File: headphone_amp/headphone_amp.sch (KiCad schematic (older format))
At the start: 40 parts, among them J1 Molex_SL_01x02_Male, J2 Molex_SL_01x02_Male, J3 Molex_SL_01x03_Male, J4 Molex_SL_01x03_Male, Q1 PZTA42, Q2 PZTA92, Q3 PZTA42, Q4 PZTA92, U1 NE5532

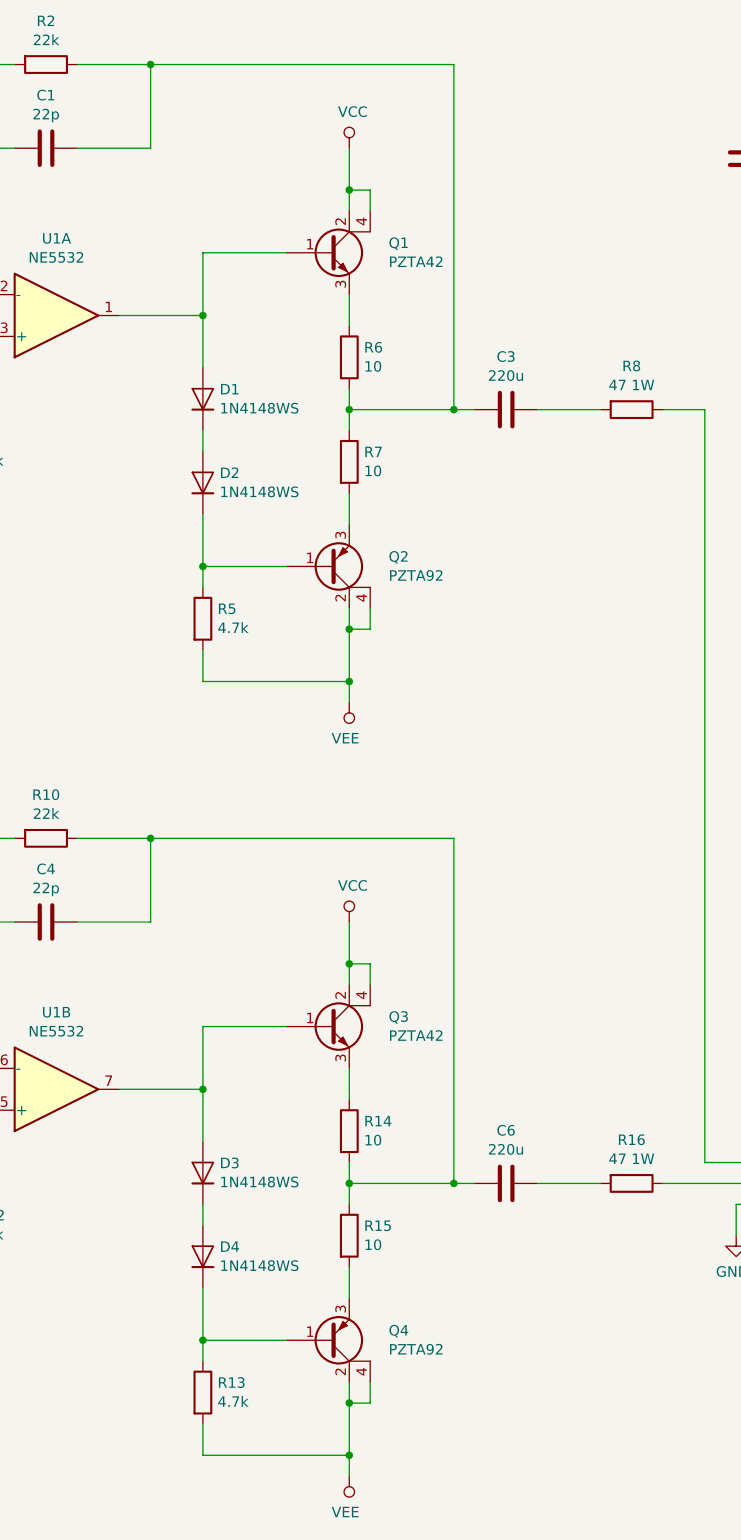
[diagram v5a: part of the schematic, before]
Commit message: update output transistor symbols/footprints
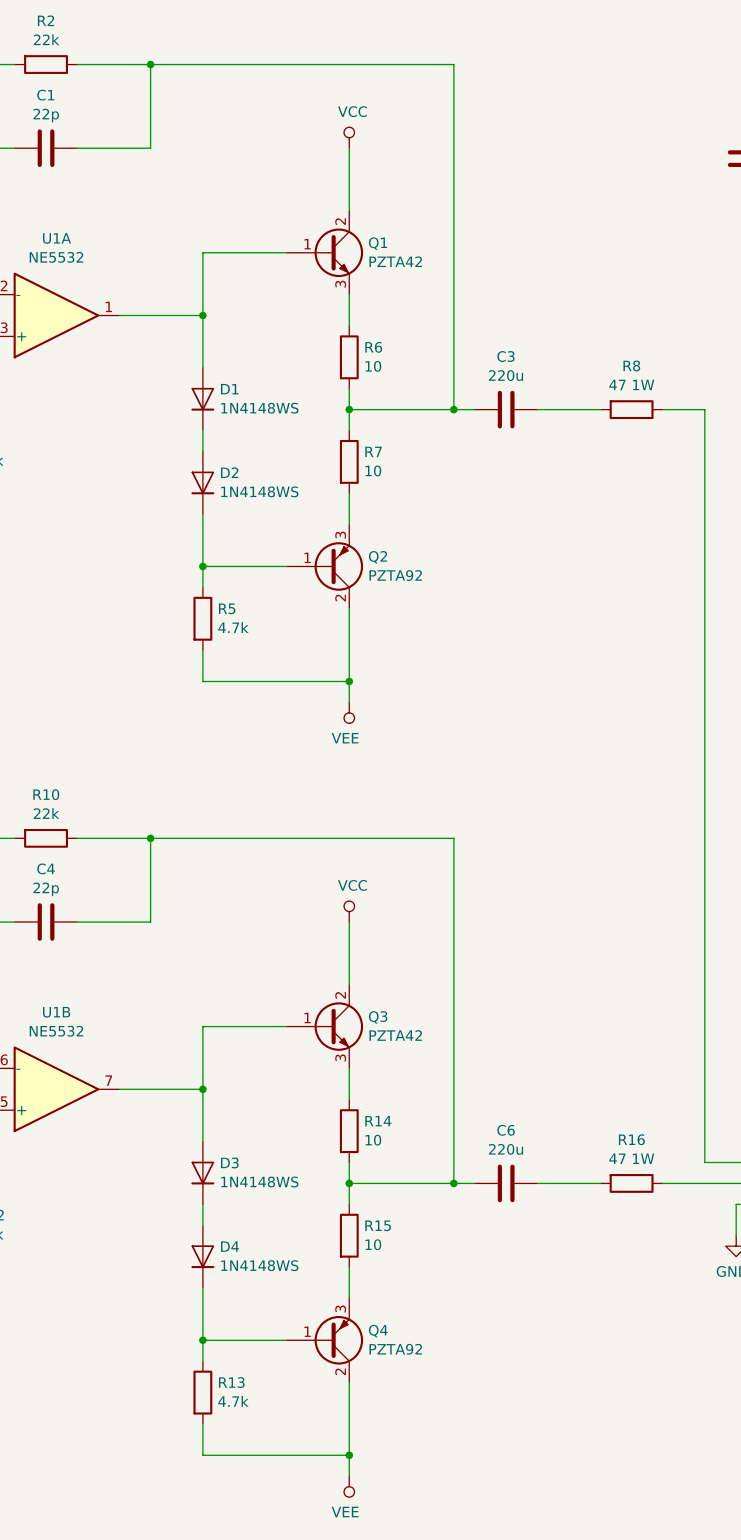
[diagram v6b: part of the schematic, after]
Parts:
- removed Q1, Q3: PZTA42, Package_TO_SOT_SMD:SOT-223, symbol Device:Q_NPN_BCEC
- removed Q2, Q4: PZTA92, Package_TO_SOT_SMD:SOT-223, symbol Device:Q_PNP_BCEC
- added Q1, Q3: PZTA42, Package_TO_SOT_SMD:SOT-223-3_TabPin2, symbol Transistor_BJT_gkeeth:PZTA42
- added Q2, Q4: PZTA92, Package_TO_SOT_SMD:SOT-223-3_TabPin2, symbol Transistor_BJT:PZTA92
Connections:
- net VCC: now also Q1.2 (C), Q3.2 (C)
- net VEE: now also Q2.2 (C), Q4.2 (C)
- net at R6.1: now also Q1.3 (E)
- net at R7.2: now also Q2.3 (E)
- net at D1.2 (A), U1.1: now also Q1.1 (B)
- net at D2.1 (K), R5.1: now also Q2.1 (B)
- net at R14.1: now also Q3.3 (E)
- net at R15.2: now also Q4.3 (E)
- net at D3.2 (A), U1.7: now also Q3.1 (B)
- net at D4.1 (K), R13.1: now also Q4.1 (B)
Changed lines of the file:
@@
 	4600 2650 4600 2750
-Wire Wire Line
-	4600 3050 4600 3300
-Wire Wire Line
-	5000 3300 4600 3300
-Connection ~ 4600 3300
-Wire Wire Line
-	4600 3300 4600 3400
-Wire Wire Line
-	5300 3100 5300 2950
 Wire Wire Line
 	5300 2650 5300 2550
@@
 Wire Wire Line
 	4600 3850 5300 3850
-Connection ~ 5300 3850
-Wire Wire Line
-	5300 3850 5300 3600
-Wire Wire Line
-	5300 1600 5300 1500
 $Comp
 L Device:R R2
@@
 	4600 7550 5300 7550
 Connection ~ 5300 7550
-Wire Wire Line
-	5300 7550 5300 7300
-Wire Wire Line
-	5300 5300 5300 5200
 $Comp
 L Device:R R12
@@
 $EndComp
 $Comp
-L Device:Q_PNP_BCEC Q2
-U 1 1 5D96CA9F
-P 5200 3300
-F 0 "Q2" H 5488 3254 50  0000 L CNN
-F 1 "PZTA92" H 5488 3345 50  0000 L CNN
-F 2 "Package_TO_SOT_SMD:SOT-223" H 5400 3400 50  0001 C CNN
-F 3 "https://www.onsemi.com/pub/Collateral/PZTA92T1-D.PDF" H 5200 3300 50  0001 C CNN
-F 4 "ON Semiconductor" H 5200 3300 50  0001 C CNN "Manufacturer"
-F 5 "PZTA92T1G" H 5200 3300 50  0001 C CNN "Manufacturer PN"
-F 6 "Digikey" H 5200 3300 50  0001 C CNN "Distributor"
-F 7 "PZTA92T1GOSCT-ND" H 5200 3300 50  0001 C CNN "Distributor PN"
-F 8 "https://www.digikey.com/product-detail/en/on-semiconductor/PZTA92T1G/PZTA92T1GOSCT-ND/920290" H 5200 3300 50  0001 C CNN "URL"
-F 9 "0.44" H 5200 3300 50  0001 C CNN "Unit Price"
-	1    5200 3300
-	1    0    0    1
-$EndComp
-$Comp
-L Device:Q_NPN_BCEC Q3
-U 1 1 5D973B3C
-P 5200 5500
-F 0 "Q3" H 5488 5546 50  0000 L CNN
-F 1 "PZTA42" H 5488 5455 50  0000 L CNN
-F 2 "Package_TO_SOT_SMD:SOT-223" H 5400 5600 50  0001 C CNN
-F 3 "https://www.onsemi.com/pub/Collateral/PZTA42T1-D.PDF" H 5200 5500 50  0001 C CNN
-F 4 "ON Semiconductor" H 5200 5500 50  0001 C CNN "Manufacturer"
-F 5 "Digikey" H 5200 5500 50  0001 C CNN "Distributor"
-F 6 "PZTA42T1GOSCT-ND" H 5200 5500 50  0001 C CNN "Distributor PN"
-F 7 "PZTA42T1G" H 5200 5500 50  0001 C CNN "Manufacturer PN"
-F 8 "https://www.digikey.com/product-detail/en/on-semiconductor/PZTA42T1G/PZTA42T1GOSCT-ND/1139989" H 5200 5500 50  0001 C CNN "URL"
-F 9 "0.43" H 5200 5500 50  0001 C CNN "Unit Price"
-	1    5200 5500
-	1    0    0    -1
-$EndComp
-Wire Wire Line
-	5300 5200 5400 5200
-Wire Wire Line
-	5400 5200 5400 5300
-Connection ~ 5300 5200
-Wire Wire Line
-	5300 5200 5300 5000
-$Comp
-L Device:Q_NPN_BCEC Q1
-U 1 1 5D97BBB9
-P 5200 1800
-F 0 "Q1" H 5488 1846 50  0000 L CNN
-F 1 "PZTA42" H 5488 1755 50  0000 L CNN
-F 2 "Package_TO_SOT_SMD:SOT-223" H 5400 1900 50  0001 C CNN
-F 3 "https://www.onsemi.com/pub/Collateral/PZTA42T1-D.PDF" H 5200 1800 50  0001 C CNN
-F 4 "ON Semiconductor" H 5200 1800 50  0001 C CNN "Manufacturer"
-F 5 "Digikey" H 5200 1800 50  0001 C CNN "Distributor"
-F 6 "PZTA42T1GOSCT-ND" H 5200 1800 50  0001 C CNN "Distributor PN"
-F 7 "PZTA42T1G" H 5200 1800 50  0001 C CNN "Manufacturer PN"
-F 8 "https://www.digikey.com/product-detail/en/on-semiconductor/PZTA42T1G/PZTA42T1GOSCT-ND/1139989" H 5200 1800 50  0001 C CNN "URL"
-F 9 "0.43" H 5200 1800 50  0001 C CNN "Unit Price"
-	1    5200 1800
-	1    0    0    -1
-$EndComp
-Wire Wire Line
-	5400 1600 5400 1500
-Wire Wire Line
-	5400 1500 5300 1500
-Connection ~ 5300 1500
-Wire Wire Line
-	5300 1500 5300 1300
-$Comp
-L Device:Q_PNP_BCEC Q4
-U 1 1 5D98233C
-P 5200 7000
-F 0 "Q4" H 5488 6954 50  0000 L CNN
-F 1 "PZTA92" H 5488 7045 50  0000 L CNN
-F 2 "Package_TO_SOT_SMD:SOT-223" H 5400 7100 50  0001 C CNN
-F 3 "https://www.onsemi.com/pub/Collateral/PZTA92T1-D.PDF" H 5200 7000 50  0001 C CNN
-F 4 "ON Semiconductor" H 5200 7000 50  0001 C CNN "Manufacturer"
-F 5 "PZTA92T1G" H 5200 7000 50  0001 C CNN "Manufacturer PN"
-F 6 "Digikey" H 5200 7000 50  0001 C CNN "Distributor"
-F 7 "PZTA92T1GOSCT-ND" H 5200 7000 50  0001 C CNN "Distributor PN"
-F 8 "https://www.digikey.com/product-detail/en/on-semiconductor/PZTA92T1G/PZTA92T1GOSCT-ND/920290" H 5200 7000 50  0001 C CNN "URL"
-F 9 "0.44" H 5200 7000 50  0001 C CNN "Unit Price"
-	1    5200 7000
-	1    0    0    1
-$EndComp
-Wire Wire Line
-	5400 3500 5400 3600
-Wire Wire Line
-	5400 3600 5300 3600
-Connection ~ 5300 3600
-Wire Wire Line
-	5300 3600 5300 3500
-Wire Wire Line
-	5400 7200 5400 7300
-Wire Wire Line
-	5400 7300 5300 7300
-Connection ~ 5300 7300
-Wire Wire Line
-	5300 7300 5300 7200
-$Comp
 L Device:R R16
 U 1 1 5D99AC16
@@
 	0    1    1    0
 $EndComp
+Wire Wire Line
+	5300 1300 5300 1600
+$Comp
+L Transistor_BJT_gkeeth:PZTA42 Q1
+U 1 1 5D835D77
+P 5200 1800
+F 0 "Q1" H 5390 1846 50  0000 L CNN
+F 1 "PZTA42" H 5390 1755 50  0000 L CNN
+F 2 "Package_TO_SOT_SMD:SOT-223-3_TabPin2" H 5400 1725 50  0001 L CIN
+F 3 "https://www.onsemi.com/pub/Collateral/PZTA42T1-D.PDF" H 5200 1800 50  0001 L CNN
+F 4 "Digikey" H 5200 1800 50  0001 C CNN "Distributor"
+F 5 "PZTA42T1GOSCT-ND" H 5200 1800 50  0001 C CNN "Distributor PN"
+F 6 "ON Semiconductor" H 5200 1800 50  0001 C CNN "Manufacturer"
+F 7 "PZTA42T1G" H 5200 1800 50  0001 C CNN "Manufacturer PN"
+F 8 "https://www.digikey.com/product-detail/en/on-semiconductor/PZTA42T1G/PZTA42T1GOSCT-ND/1139989" H 5200 1800 50  0001 C CNN "URL"
+F 9 "0.43" H 5200 1800 50  0001 C CNN "Unit Price"
+	1    5200 1800
+	1    0    0    -1
+$EndComp
+Connection ~ 5300 3850
+Wire Wire Line
+	5300 3100 5300 2950
+Wire Wire Line
+	4600 3300 4600 3400
+Wire Wire Line
+	4600 3050 4600 3300
+Connection ~ 4600 3300
+Wire Wire Line
+	5000 3300 4600 3300
+$Comp
+L Transistor_BJT:PZTA92 Q2
+U 1 1 5D83FFA6
+P 5200 3300
+F 0 "Q2" H 5390 3254 50  0000 L CNN
+F 1 "PZTA92" H 5390 3345 50  0000 L CNN
+F 2 "Package_TO_SOT_SMD:SOT-223-3_TabPin2" H 5400 3225 50  0001 L CIN
+F 3 "https://www.onsemi.com/pub/Collateral/PZTA92T1-D.PDF" H 5200 3300 50  0001 L CNN
+F 4 "Digikey" H 5200 3300 50  0001 C CNN "Distributor"
+F 5 "PZTA92T1GOSCT-ND" H 5200 3300 50  0001 C CNN "Distributor PN"
+F 6 "ON Semiconductor" H 5200 3300 50  0001 C CNN "Manufacturer"
+F 7 "PZTA92T1G" H 5200 3300 50  0001 C CNN "Manufacturer PN"
+F 8 "https://www.digikey.com/product-detail/en/on-semiconductor/PZTA92T1G/PZTA92T1GOSCT-ND/920290" H 5200 3300 50  0001 C CNN "URL"
+F 9 "0.44" H 5200 3300 50  0001 C CNN "Unit Price"
+	1    5200 3300
+	1    0    0    1
+$EndComp
+Wire Wire Line
+	5300 3500 5300 3850
+Wire Wire Line
+	5300 7200 5300 7550
+Wire Wire Line
+	5300 5000 5300 5300
+$Comp
+L Transistor_BJT:PZTA92 Q4
+U 1 1 5D846814
+P 5200 7000
+F 0 "Q4" H 5390 6954 50  0000 L CNN
+F 1 "PZTA92" H 5390 7045 50  0000 L CNN
+F 2 "Package_TO_SOT_SMD:SOT-223-3_TabPin2" H 5400 6925 50  0001 L CIN
+F 3 "https://www.onsemi.com/pub/Collateral/PZTA92T1-D.PDF" H 5200 7000 50  0001 L CNN
+F 4 "Digikey" H 5200 7000 50  0001 C CNN "Distributor"
+F 5 "PZTA92T1GOSCT-ND" H 5200 7000 50  0001 C CNN "Distributor PN"
+F 6 "ON Semiconductor" H 5200 7000 50  0001 C CNN "Manufacturer"
+F 7 "PZTA92T1G" H 5200 7000 50  0001 C CNN "Manufacturer PN"
+F 8 "https://www.digikey.com/product-detail/en/on-semiconductor/PZTA92T1G/PZTA92T1GOSCT-ND/920290" H 5200 7000 50  0001 C CNN "URL"
+F 9 "0.44" H 5200 7000 50  0001 C CNN "Unit Price"
+	1    5200 7000
+	1    0    0    1
+$EndComp
+$Comp
+L Transistor_BJT_gkeeth:PZTA42 Q3
+U 1 1 5D8472CD
+P 5200 5500
+F 0 "Q3" H 5390 5546 50  0000 L CNN
+F 1 "PZTA42" H 5390 5455 50  0000 L CNN
+F 2 "Package_TO_SOT_SMD:SOT-223-3_TabPin2" H 5400 5425 50  0001 L CIN
+F 3 "https://www.onsemi.com/pub/Collateral/PZTA42T1-D.PDF" H 5200 5500 50  0001 L CNN
+F 4 "Digikey" H 5200 5500 50  0001 C CNN "Distributor"
+F 5 "PZTA42T1GOSCT-ND" H 5200 5500 50  0001 C CNN "Distributor PN"
+F 6 "ON Semiconductor" H 5200 5500 50  0001 C CNN "Manufacturer"
+F 7 "PZTA42T1G" H 5200 5500 50  0001 C CNN "Manufacturer PN"
+F 8 "https://www.digikey.com/product-detail/en/on-semiconductor/PZTA42T1G/PZTA42T1GOSCT-ND/1139989" H 5200 5500 50  0001 C CNN "URL"
+F 9 "0.43" H 5200 5500 50  0001 C CNN "Unit Price"
+	1    5200 5500
+	1    0    0    -1
+$EndComp
 $EndSCHEMATC

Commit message: change output transistors to std lib versions (now in upstream)
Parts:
- removed Q1, Q3: PZTA42, Package_TO_SOT_SMD:SOT-223-3_TabPin2, symbol Transistor_BJT_gkeeth:PZTA42
- added Q1, Q3: PZTA42, Package_TO_SOT_SMD:SOT-223-3_TabPin2, symbol Transistor_BJT:PZTA42
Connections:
- net VCC: now also Q1.2 (C), Q3.2 (C)
- net at R6.1: now also Q1.3 (E)
- net at D1.2 (A), U1.1: now also Q1.1 (B)
- net at R14.1: now also Q3.3 (E)
- net at D3.2 (A), U1.7: now also Q3.1 (B)
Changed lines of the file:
@@
 Wire Wire Line
 	5300 1300 5300 1600
+Connection ~ 5300 3850
+Wire Wire Line
+	5300 3100 5300 2950
+Wire Wire Line
+	4600 3300 4600 3400
+Wire Wire Line
+	4600 3050 4600 3300
+Connection ~ 4600 3300
+Wire Wire Line
+	5000 3300 4600 3300
+Wire Wire Line
+	5300 3500 5300 3850
+Wire Wire Line
+	5300 7200 5300 7550
+Wire Wire Line
+	5300 5000 5300 5300
 $Comp
-L Transistor_BJT_gkeeth:PZTA42 Q1
-U 1 1 5D835D77
+L Transistor_BJT:PZTA42 Q1
+U 1 1 5D86B1D4
 P 5200 1800
 F 0 "Q1" H 5390 1846 50  0000 L CNN
@@
 	1    0    0    -1
 $EndComp
-Connection ~ 5300 3850
-Wire Wire Line
-	5300 3100 5300 2950
-Wire Wire Line
-	4600 3300 4600 3400
-Wire Wire Line
-	4600 3050 4600 3300
-Connection ~ 4600 3300
-Wire Wire Line
-	5000 3300 4600 3300
 $Comp
 L Transistor_BJT:PZTA92 Q2
-U 1 1 5D83FFA6
+U 1 1 5D86C06E
 P 5200 3300
 F 0 "Q2" H 5390 3254 50  0000 L CNN
@@
 	1    0    0    1
 $EndComp
-Wire Wire Line
-	5300 3500 5300 3850
-Wire Wire Line
-	5300 7200 5300 7550
-Wire Wire Line
-	5300 5000 5300 5300
+$Comp
+L Transistor_BJT:PZTA42 Q3
+U 1 1 5D86E452
+P 5200 5500
+F 0 "Q3" H 5390 5546 50  0000 L CNN
+F 1 "PZTA42" H 5390 5455 50  0000 L CNN
+F 2 "Package_TO_SOT_SMD:SOT-223-3_TabPin2" H 5400 5425 50  0001 L CIN
+F 3 "https://www.onsemi.com/pub/Collateral/PZTA42T1-D.PDF" H 5200 5500 50  0001 L CNN
+F 4 "Digikey" H 5200 5500 50  0001 C CNN "Distributor"
+F 5 "PZTA42T1GOSCT-ND" H 5200 5500 50  0001 C CNN "Distributor PN"
+F 6 "ON Semiconductor" H 5200 5500 50  0001 C CNN "Manufacturer"
+F 7 "PZTA42T1G" H 5200 5500 50  0001 C CNN "Manufacturer PN"
+F 8 "https://www.digikey.com/product-detail/en/on-semiconductor/PZTA42T1G/PZTA42T1GOSCT-ND/1139989" H 5200 5500 50  0001 C CNN "URL"
+F 9 "0.43" H 5200 5500 50  0001 C CNN "Unit Price"
+	1    5200 5500
+	1    0    0    -1
+$EndComp
 $Comp
 L Transistor_BJT:PZTA92 Q4
-U 1 1 5D846814
+U 1 1 5D86F45B
 P 5200 7000
 F 0 "Q4" H 5390 6954 50  0000 L CNN
@@
 	1    0    0    1
 $EndComp
-$Comp
-L Transistor_BJT_gkeeth:PZTA42 Q3
-U 1 1 5D8472CD
-P 5200 5500
-F 0 "Q3" H 5390 5546 50  0000 L CNN
-F 1 "PZTA42" H 5390 5455 50  0000 L CNN
-F 2 "Package_TO_SOT_SMD:SOT-223-3_TabPin2" H 5400 5425 50  0001 L CIN
-F 3 "https://www.onsemi.com/pub/Collateral/PZTA42T1-D.PDF" H 5200 5500 50  0001 L CNN
-F 4 "Digikey" H 5200 5500 50  0001 C CNN "Distributor"
-F 5 "PZTA42T1GOSCT-ND" H 5200 5500 50  0001 C CNN "Distributor PN"
-F 6 "ON Semiconductor" H 5200 5500 50  0001 C CNN "Manufacturer"
-F 7 "PZTA42T1G" H 5200 5500 50  0001 C CNN "Manufacturer PN"
-F 8 "https://www.digikey.com/product-detail/en/on-semiconductor/PZTA42T1G/PZTA42T1GOSCT-ND/1139989" H 5200 5500 50  0001 C CNN "URL"
-F 9 "0.43" H 5200 5500 50  0001 C CNN "Unit Price"
-	1    5200 5500
-	1    0    0    -1
-$EndComp
 $EndSCHEMATC

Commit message: Remove output resistors
- remove output resistors for zero ohm output impedance
- add 10k pulldown/bleeder resistors on output to prevent output cap
charging with no load
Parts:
- R16, R8: value 47 1W -> 10k; footprint Resistor_THT:R_Axial_DIN0414_L11.9mm_D4.5mm_P15.24mm_Horizontal -> Resistor_SMD:R_0603_1608Metric_Pad1.05x0.95mm_HandSolder; Distributor Digikey -> (none); Distributor PN BC4537CT-ND -> (none); Manufacturer Vishay BC -> (none); Manufacturer PN MBE04140C4709FC100 -> (none); URL https://www.digikey.com/product-detail/en/vishay-bc-compone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 -> (none); Unit Price 0.69 -> (none)
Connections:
- net GNDA: now also R16.2, R8.2
- net left_out: now also C3.1
- net right_out: now also C6.1
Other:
- note added: "TODO\nconsider other opamps, especially lm4562 and TL072\nheadphone jack ground to chassis...?\nadjust system gain to match headphone volume to speaker volume"
- note added: "adjust gain"
- note removed: "TODO\nconsider other opamps, especially lm4562 and TL072\nheadphone jack ground to chassis...?"
- moved on the sheet: C4, C5, C6, D3, D4, J2, J3, J4, Q3, Q4, R10, R11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
